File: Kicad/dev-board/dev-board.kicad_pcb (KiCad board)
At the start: 2 copper layers, 100 x 70 mm, 59 parts, among them J1 Conn_01x03_Male, J10 Conn_01x03_Male, J11 Conn_01x03_Male, J13 Conn_01x04_Male, J15 Conn_01x03_Male, J16 Conn_01x06_Male, J2 Conn_01x04_Male, J3 Conn_01x02_Male, J4 Conn_01x02_Male, J5 Conn_01x02_Male, J6 Conn_01x02_Male, J7 Conn_01x04_Male, J8 Conn_01x03_Male, J9 Conn_01x03_Male, Q1 2N2219, SW1 SW_DIP_x04, SW2 SW_SPDT, SW3 SW_SPDT, SW4 SW_Push, SW5 SW_Push, SW6 SW_Push, SW7 SW_Push, SW8 Rotary_Encoder_Switch, U1 NE555P

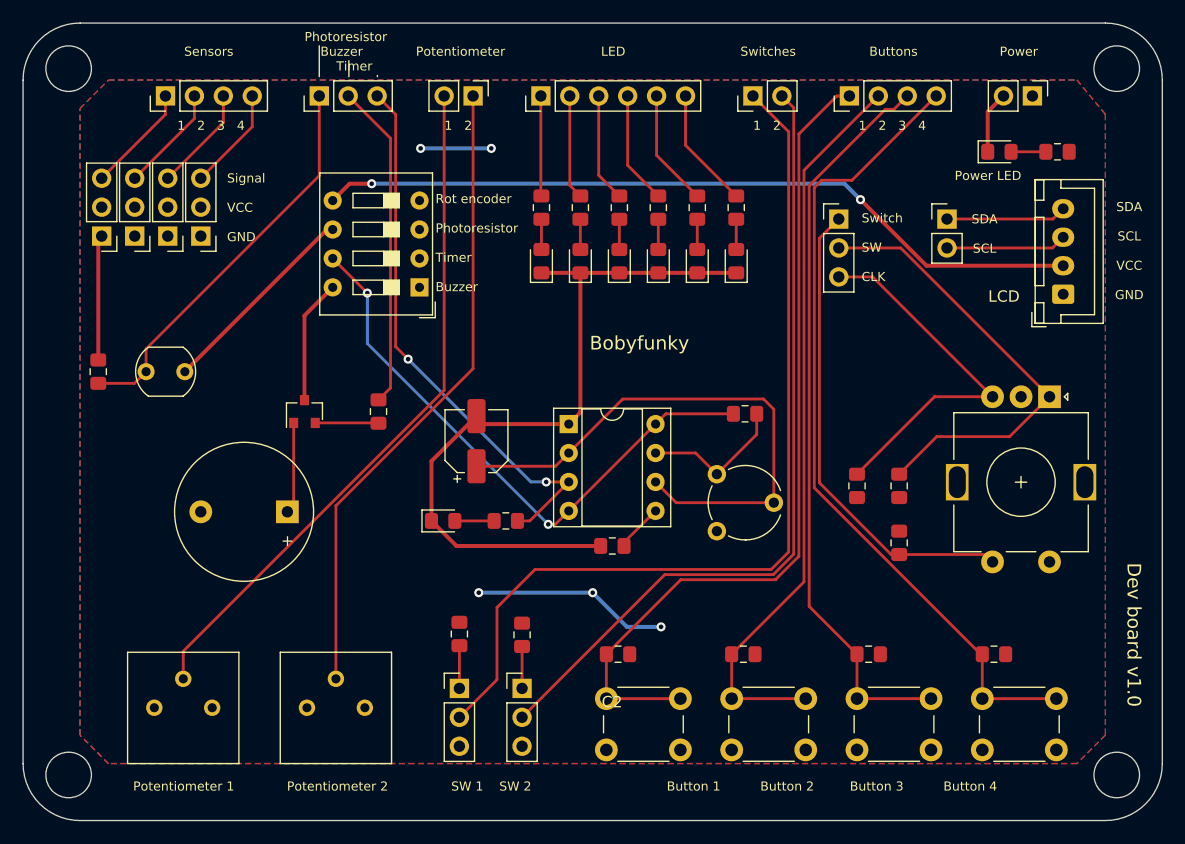
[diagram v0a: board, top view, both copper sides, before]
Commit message: Drill holes
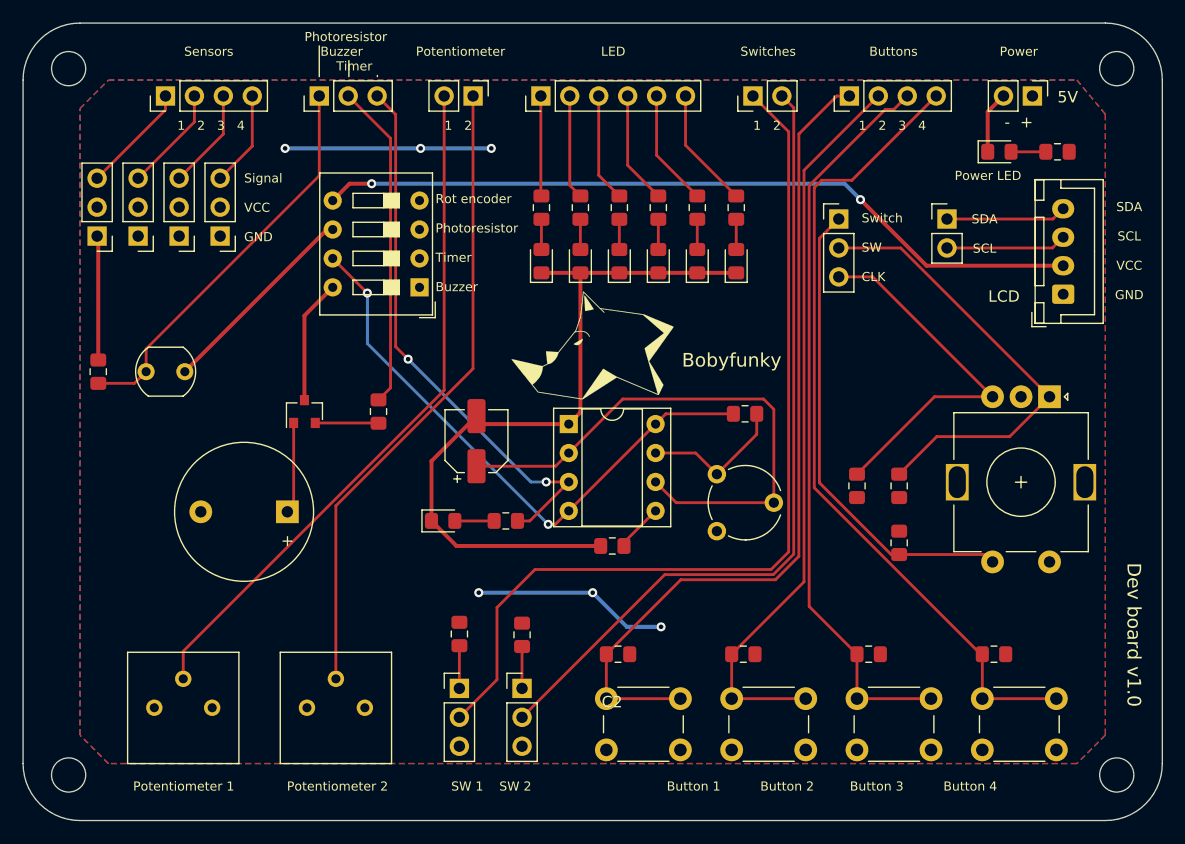
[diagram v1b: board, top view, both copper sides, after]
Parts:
- added G***: LOGO, Logo:logo_15mm, F.Cu at (150.0, 78.3)
- added G***: LOGO, Logo:logo_30mm, B.Cu at (154.3, 70.4)
- added REF**: MountingHole_3mm, MountingHole:MountingHole_3mm, F.Cu at (196.0, 54.0)
- added REF**: MountingHole_3mm, MountingHole:MountingHole_3mm, F.Cu at (196.0, 116.0)
- added REF**: MountingHole_3mm, MountingHole:MountingHole_3mm, F.Cu at (104.0, 116.0)
- added REF**: MountingHole_3mm, MountingHole:MountingHole_3mm, F.Cu at (104.0, 54.0)
- added REF**: OSHW-Symbol_8.9x8mm_SilkScreen, Symbol:OSHW-Symbol_8.9x8mm_SilkScreen, B.Cu at (127.7, 100.8)
- added REF**: WEEE-Logo_5.6x8mm_SilkScreen, Symbol:WEEE-Logo_5.6x8mm_SilkScreen, B.Cu at (114.1, 100.6)
- moved J11 1.70 mm to (117.3, 68.7)
- moved J10 1.00 mm to (113.7, 68.7)
- moved J8 0.40 mm to (106.5, 68.7)
- moved J9 0.30 mm to (110.1, 68.7)
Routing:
- net VCC: track 23.4 -> 35.3 mm, vias 5 -> 6
- net Net-(J11-Pad3): track 9.09 -> 8.39 mm
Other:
- outline, holes or cut-outs redrawn
- board text added: "- +"
- board text added: "5V"

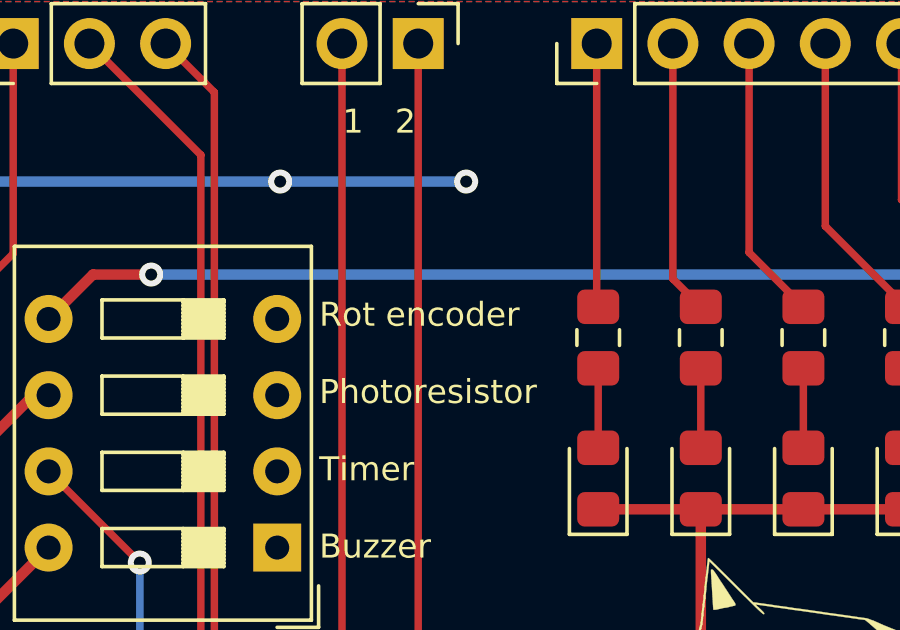
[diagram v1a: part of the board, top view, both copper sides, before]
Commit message: Add components values
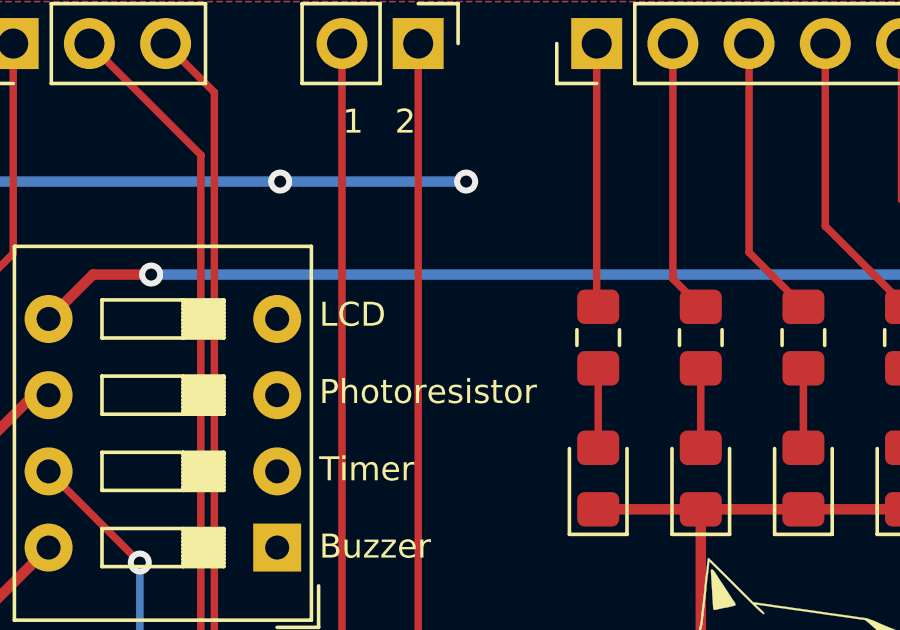
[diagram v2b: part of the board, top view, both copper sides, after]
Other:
- board text added: "LCD Photoresistor Timer Buzzer"
- board text removed: "Rot encoder Photoresistor Timer Buzzer"
